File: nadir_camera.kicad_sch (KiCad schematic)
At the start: 54 parts, among them J1 MOLEX_5051102491, J12 Conn 02x05 1.27mm, J13 Micro_SD_Card, J14 USB_C_Receptacle_USB2.0, SW5 KMR2x, SW6 CAS-120TA, U24 STM32H743VITx, U25 USBLC6-2SC6, Y4 12MHz/7pF

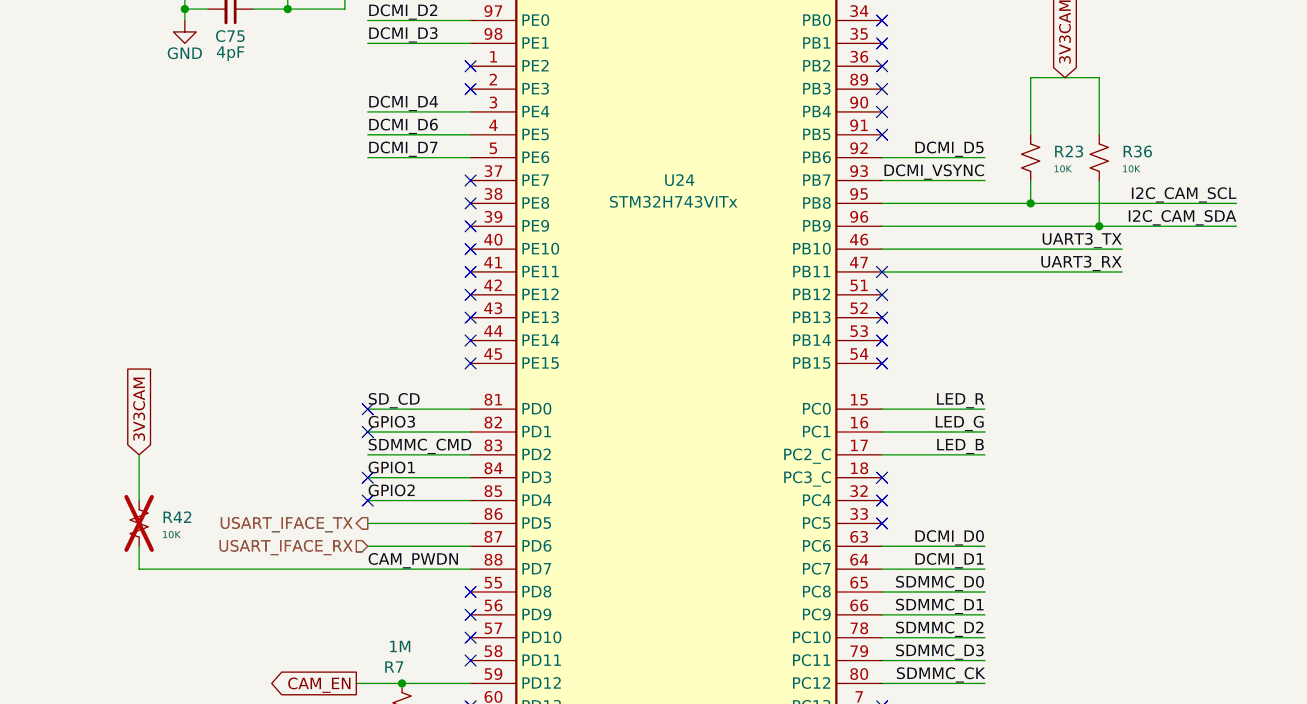
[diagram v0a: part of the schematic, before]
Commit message: Add MPNs for all parts
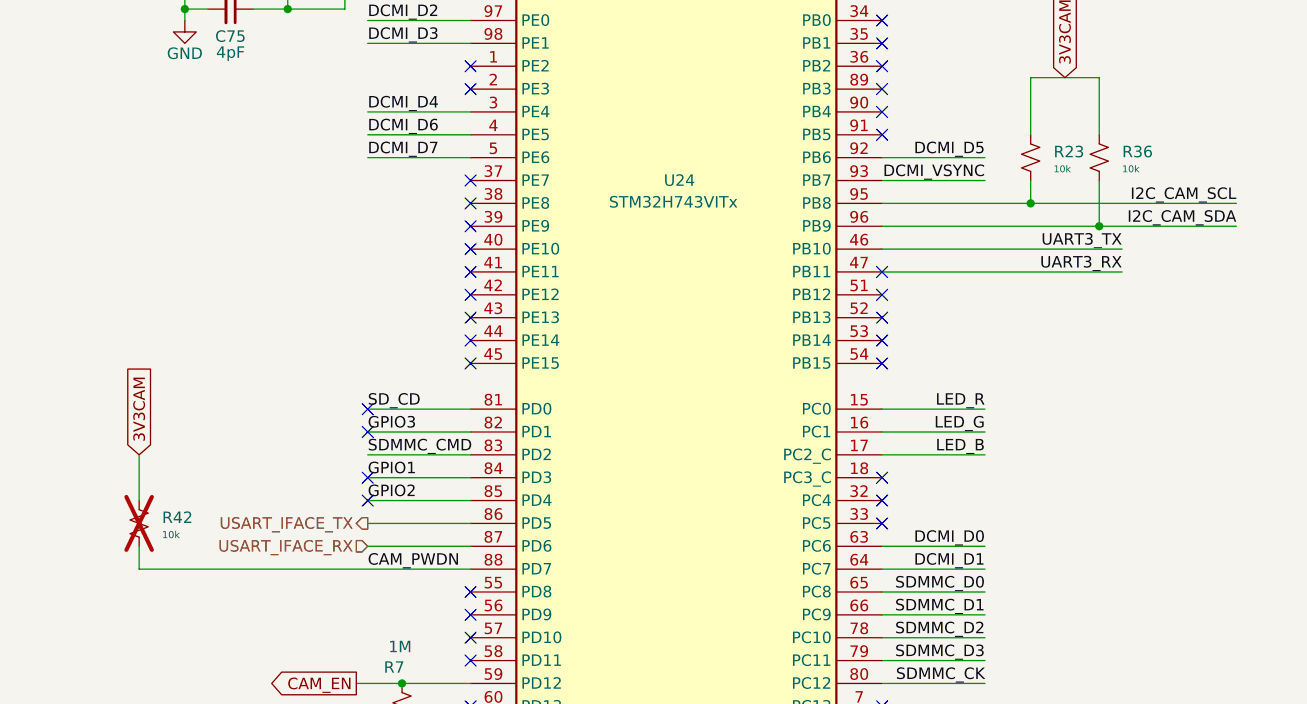
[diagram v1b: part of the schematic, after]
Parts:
- C17, C20: Manufacturer_Part_Number GRT188R61C106ME13D -> GCM188R71E105KA64D
- C62: Manufacturer_Part_Number (none) -> C1206C476M8PAC7800
- C63, C64, C65, C66, C67, C68: Manufacturer_Part_Number (none) -> GCM188L81H104KA57D
- C69: Manufacturer_Part_Number (none) -> GCM188R72A103KA37D
- C70, C71: Manufacturer_Part_Number (none) -> GCM188R71E105KA64D
- C72, C73: Manufacturer_Part_Number (none) -> GCM188R70J225KE22D
- C74, C75: Manufacturer_Part_Number (none) -> CGA3E2C0G1H040C080AA
- FB3: Manufacturer_Part_Number (none) -> BLM18SG121TZ1D
- R23, R36, R42: value 10K -> 10k; Manufacturer_Part_Number (none) -> ERJ-3EKF1002V
- R43: Manufacturer_Part_Number (none) -> ERJ-3EKF1004V
- U24: Manufacturer_Part_Number (none) -> STM32H743VIT6
- Y4: Manufacturer_Part_Number (none) -> ECS-120-7-36Q-AEY-TR
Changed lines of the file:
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@@
 			)
 		)
+		(property "Manufacturer_Part_Number" "GCM188R71E105KA64D"
+			(at 143.51 41.91 0)
+			(effects
+				(font
+					(size 1.27 1.27)
+				)
+				(hide yes)
+			)
+		)
 		(pin "1"
 		)
@@
 			)
 		)
+		(property "Manufacturer_Part_Number" "GCM188L81H104KA57D"
+			(at 35.56 41.91 0)
+			(effects
+				(font
+					(size 1.27 1.27)
+				)
+				(hide yes)
+			)
+		)
 		(pin "1"
 		)
@@
 			)
 		)
+		(property "Manufacturer_Part_Number" "GCM188R70J225KE22D"
+			(at 50.8 69.85 0)
+			(effects
+				(font
+					(size 1.27 1.27)
+				)
+				(hide yes)
+			)
+		)
 		(pin "1"
 		)
@@
 			)
 		)
+		(property "Manufacturer_Part_Number" "ERJ-3EKF1004V"
+			(at 252.73 41.91 0)
+			(effects
+				(font
+					(size 1.27 1.27)
+				)
+				(hide yes)
+			)
+		)
 		(pin "2"
 		)
@@
 			)
 		)
+		(property "Manufacturer_Part_Number" "C1206C476M8PAC7800"
+			(at 26.67 41.91 0)
+			(effects
+				(font
+					(size 1.27 1.27)
+				)
+				(hide yes)
+			)
+		)
 		(pin "1"
 		)
@@
 			)
 		)
+		(property "Manufacturer_Part_Number" "GCM188L81H104KA57D"
+			(at 85.09 41.91 0)
+			(effects
+				(font
+					(size 1.27 1.27)
+				)
+				(hide yes)
+			)
+		)
 		(pin "1"
 		)
@@
 			)
 		)
+		(property "Manufacturer_Part_Number" "CGA3E2C0G1H040C080AA"
+			(at 50.8 95.25 0)
+			(effects
+				(font
+					(size 1.27 1.27)
+				)
+				(hide yes)
+			)
+		)
 		(pin "1"
 		)
@@
 			)
 		)
-		(property "Manufacturer_Part_Number" "GRT188R61C106ME13D"
+		(property "Manufacturer_Part_Number" "GCM188R71E105KA64D"
 			(at 340.36 102.87 0)
 			(effects
@@
 			)
 		)
+		(property "Manufacturer_Part_Number" "GCM188L81H104KA57D"
+			(at 74.93 41.91 0)
+			(effects
+				(font
+					(size 1.27 1.27)
+				)
+				(hide yes)
+			)
+		)
 		(pin "1"
 		)
@@
 			)
 		)
-		(property "Manufacturer_Part_Number" "GRT188R61C106ME13D"
+		(property "Manufacturer_Part_Number" "GCM188R71E105KA64D"
 			(at 318.77 102.87 0)
 			(effects
@@
 			)
 		)
+		(property "Manufacturer_Part_Number" "GCM188R71E105KA64D"
+			(at 125.73 41.91 0)
+			(effects
+				(font
+					(size 1.27 1.27)
+				)
+				(hide yes)
+			)
+		)
 		(pin "1"
 		)
@@
 			)
 		)
+		(property "Manufacturer_Part_Number" "GCM188R72A103KA37D"
+			(at 115.57 41.91 0)
+			(effects
+				(font
+					(size 1.27 1.27)
+				)
+				(hide yes)
+			)
+		)
 		(pin "1"
 		)
@@
 			)
 		)
-		(property "Value" "10K"
+		(property "Value" "10k"
 			(at 149.86 113.03 0)
 			(effects
@@
 			)
 		)
+		(property "Manufacturer_Part_Number" "ERJ-3EKF1002V"
+			(at 147.32 111.76 0)
+			(effects
+				(font
+					(size 1.27 1.27)
+				)
+				(hide yes)
+			)
+		)
 		(pin "1"
 		)
@@
 			)
 		)
+		(property "Manufacturer_Part_Number" "GCM188L81H104KA57D"
+			(at 55.88 41.91 0)
+			(effects
+				(font
+					(size 1.27 1.27)
+				)
+				(hide yes)
+			)
+		)
 		(pin "1"
 		)
@@
 			)
 		)
+		(property "Manufacturer_Part_Number" "GCM188L81H104KA57D"
+			(at 66.04 41.91 0)
+			(effects
+				(font
+					(size 1.27 1.27)
+				)
+				(hide yes)
+			)
+		)
 		(pin "1"
 		)
@@
 			)
 		)
+		(property "Manufacturer_Part_Number" "GCM188L81H104KA57D"
+			(at 45.72 41.91 0)
+			(effects
+				(font
+					(size 1.27 1.27)
+				)
+				(hide yes)
+			)
+		)
 		(pin "1"
 		)
@@
 			)
 		)
+		(property "Manufacturer_Part_Number" "CGA3E2C0G1H040C080AA"
+			(at 50.8 85.09 0)
+			(effects
+				(font
+					(size 1.27 1.27)
+				)
+				(hide yes)
+			)
+		)
 		(pin "1"
 		)
@@
 			)
 		)
+		(property "Manufacturer_Part_Number" "STM32H743VIT6"
+			(at 100.33 114.3 0)
+			(effects
+				(font
+					(size 1.27 1.27)
+				)
+				(hide yes)
+			)
+		)
 		(pin "1"
 		)
@@
 			)
 		)
+		(property "Manufacturer_Part_Number" "BLM18SG121TZ1D"
+			(at 133.35 36.83 0)
+			(effects
+				(font
+					(size 1.27 1.27)
+				)
+				(hide yes)
+			)
+		)
 		(pin "1"
 		)
@@
 			)
 		)
+		(property "Manufacturer_Part_Number" "GCM188R70J225KE22D"
+			(at 55.88 69.85 0)
+			(effects
+				(font
+					(size 1.27 1.27)
+				)
+				(hide yes)
+			)
+		)
 		(pin "1"
 		)
@@
 			)
 		)
-		(property "Value" "10K"
+		(property "Value" "10k"
 			(at 142.24 113.03 0)
 			(effects
@@
 			)
 		)
+		(property "Manufacturer_Part_Number" "ERJ-3EKF1002V"
+			(at 139.7 111.76 0)
+			(effects
+				(font
+					(size 1.27 1.27)
+				)
+				(hide yes)
+			)
+		)
 		(pin "1"
 		)
@@
 			)
 		)
+		(property "Manufacturer_Part_Number" "ECS-120-7-36Q-AEY-TR "
+			(at 57.15 90.17 0)
+			(effects
+				(font
+					(size 1.27 1.27)
+				)
+				(hide yes)
+			)
+		)
 		(pin "1"
 		)
@@
 			)
 		)
-		(property "Value" "10K"
+		(property "Value" "10k"
 			(at 43.18 153.67 0)
 			(effects
@@
 			(at 40.64 152.4 0)
 			(effects
+				(font
+					(size 1.27 1.27)
+				)
+				(hide yes)
+			)
+		)
+		(property "Manufacturer_Part_Number" "ERJ-3EKF1002V"
+			(at 40.64 152.4 0)
+			(effects

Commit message: Fix some wrong MPNs
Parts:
- C17, C20: Manufacturer_Part_Number GCM188R71E105KA64D -> GRT188R61A106KE13D
- R63: Manufacturer_Part_Number ERJ-3EKF1002V -> ESR03EZPF1000
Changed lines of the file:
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@@
 			)
 		)
-		(property "Manufacturer_Part_Number" "ERJ-3EKF1002V"
+		(property "Manufacturer_Part_Number" "ESR03EZPF1000"
 			(at 218.44 165.1 0)
 			(effects
@@
 			)
 		)
-		(property "Manufacturer_Part_Number" "GCM188R71E105KA64D"
+		(property "Manufacturer_Part_Number" "GRT188R61A106KE13D"
 			(at 340.36 102.87 0)
 			(effects
@@
 			)
 		)
-		(property "Manufacturer_Part_Number" "GCM188R71E105KA64D"
+		(property "Manufacturer_Part_Number" "GRT188R61A106KE13D"
 			(at 318.77 102.87 0)
 			(effects

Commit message: Update to single multi-core processor
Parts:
- removed C62, C78: 47uF, Capacitor_Tantalum_SMD:CP_EIA-2012-12_Kemet-R, symbol Device:C_Polarized_Small_US
- removed C63, C64, C65, C66, C67, C68, C76, C79: 0.1uF, Capacitor_SMD:C_0603_1608Metric, symbol Device:C_Small
- removed C69: 10nF, Capacitor_SMD:C_0603_1608Metric, symbol Device:C_Small
- removed C70, C71, C77: 1uF, Capacitor_SMD:C_0603_1608Metric, symbol Device:C_Small
- removed C72, C73: 2.2uF, Capacitor_SMD:C_0603_1608Metric, symbol Device:C_Small
- removed C74, C75: 4pF, Capacitor_SMD:C_0603_1608Metric, symbol Device:C_Small
- removed C80: 4.7nF, Capacitor_SMD:C_0603_1608Metric, symbol Device:C_Small
- removed FB3: 120R, Inductor_SMD:L_0603_1608Metric, symbol Device:FerriteBead_Small
- removed J12: Conn 02x05 1.27mm, Connector_PinHeader_1.27mm:PinHeader_2x05_P1.27mm_Vertical_SMD, symbol Connector_Generic:Conn_02x05_Odd_Even
- removed J13: Micro_SD_Card, mainboard:microSD_104031-0811, symbol Connector:Micro_SD_Card_Det2
- removed J14: USB_C_Receptacle_USB2.0, Connector_USB:USB_C_Receptacle_HRO_TYPE-C-31-M-12, symbol Connector:USB_C_Receptacle_USB2.0
- removed LED6: 150141M173100, LED_SMD:LED_RGB_Wuerth-PLCC4_3.2x2.8mm_150141M173100, symbol Device:LED_ABRG
- removed R23, R36, R42, R62, R64: 10k, Resistor_SMD:R_0603_1608Metric, symbol Device:R_Small_US
- removed R43, R7: 1M, Resistor_SMD:R_0603_1608Metric, symbol Device:R_Small_US
- removed R63: 100R, Resistor_SMD:R_0603_1608Metric, symbol Device:R_Small_US
- removed R65, R66, R67, R68, R69: 47k, Resistor_SMD:R_0603_1608Metric, symbol Device:R_Small_US
- removed R70, R71: 5.1k, Resistor_SMD:R_0603_1608Metric, symbol Device:R_US
- removed R72: 1M, Resistor_SMD:R_0603_1608Metric, symbol Device:R_US
- removed RN2: 330R, Resistor_SMD:R_Array_Concave_4x0603, symbol Device:R_Pack04
- removed SW5: KMR2x, mainboard:BTN_KMR2, symbol Switch:SW_Push
- removed SW6: CAS-120TA, cameraboard:CAS-120TA, symbol Switch:SW_SPDT
- removed U24: STM32H743VITx, Package_QFP:LQFP-100_14x14mm_P0.5mm, symbol MCU_ST_STM32H7:STM32H743VITx
- removed U25: USBLC6-2SC6, Package_TO_SOT_SMD:SOT-23-6, symbol Power_Protection:USBLC6-2SC6
- removed Y4: 12MHz/7pF, Crystal:Crystal_SMD_2520-4Pin_2.5x2.0mm, symbol Device:Crystal_GND24_Small
- added C28, C29: 22pF, Capacitor_SMD:C_0603_1608Metric, symbol Device:C_Small
- added C31, C7: 0.1uF, Capacitor_SMD:C_0603_1608Metric, symbol Device:C_Small
- added C33: 0.1uF, Capacitor_SMD:C_0603_1608Metric, symbol Device:C
- added R17, R21: 10k, Resistor_SMD:R_0603_1608Metric, symbol Device:R_US
- added U23: OPT4001, Package_TO_SOT_SMD:SOT-583-8, symbol solarpanels:OPT4001
- added U5: BNO085, mainboard:BNO085, symbol mainboard:BNO085
- added Y3: 32.768kHz/12.5pF, Crystal:Crystal_SMD_MicroCrystal_CC7V-T1A-2Pin_3.2x1.5mm, symbol Device:Crystal_Small
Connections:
- net GND: now also C28.1, C29.2, C31.2, C33.2, C7.2, U23.4 (GND), U5.10 (CLKSEL0), U5.17 (H_SA0/MOSI), U5.2 (GND), U5.25 (GNDIO), U5.5 (PS1), U5.6 (PS0/WAKE)
- new net: C29.1, U5.26 (CLKSEL1/XOUT32), Y3.2
- new net: U5.1 (NC), U5.12 (NC), U5.13 (NC), U5.21 (NC), U5.22 (NC), U5.23 (NC), U5.24 (NC), U5.7 (NC), U5.8 (NC)
- new net: C28.2, U5.27 (XIN32), Y3.1
- new net: R21.1, U5.4 (BOOTN)
- new net: C7.1, U5.9 (CAP)
- new net: U23.3 (NC), U23.6 (NC)
- new net +3V3: C31.1, C33.1, R17.2, R21.2, U23.1 (VDD), U23.2 (ADDR), U5.28 (VDDIO), U5.3 (VDD)
- new net I2C_IMU_SCL: U5.19 (H_SCL/SCLK/RX)
- new net I2C_IMU_SDA: U5.20 (H_SDA/MISO/TX)
- new net I2C_LIGHT2_SCL: U23.5 (SCL)
- new net I2C_LIGHT2_SDA: U23.8 (SDA)
- new net IMU_INT: U5.14 (H_INTN)
- new net IMU_RST: R17.1, U5.11 (NRST)
- no-connect marks 51 -> 7
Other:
- note added: "IMU"
- note added: "IMU datasheet recommends 12.5pF crystal capacitance"
- note added: "Nadir Light Sensor"
- note removed: "Check Xtal Datasheet This value assumes 7pF crystal bulk capacitance"
- note removed: "Datasheet: https://www.st.com/resource/en/datasheet/stm32h743vi.pdf (See pg. 209 for power supply instructions)"
- note removed: "ESR < 100 mOhm Tol < 20%"
- note removed: "MCU (STM32H743VITx)"
- note removed: "Reset & Boot0 Switches"
- note removed: "SD Card"
- note removed: "SWD CONN"
- note removed: "See https://www.st.com/resource/en/application_note/an5612-esd-protection-of-stm32-mcus-and-mpus-stmicroelectronics.pdf, p. 22"
- note removed: "Select boot mode Set "low" for normal operation. Set "high" for bootloader mode"
- note removed: "Set for flight"
- note removed: "Shield"
- note removed: "Status LEDs"
- note removed: "Status RGB LED"
- note removed: "USB Connector"
- note removed: "USB ESD Protection"

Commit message: Add USB PD battery charging circuit
Closes #1
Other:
- moved on the sheet: C16, C17, C18, C19, C20, C21, C28, C29, C31, C33, C7, FB1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

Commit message: Move things around in schematic
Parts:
- removed C16, C19: 1uF, Capacitor_SMD:C_0603_1608Metric, symbol Device:C_Small
- removed C17, C20: 10uF, Capacitor_SMD:C_0603_1608Metric, symbol Device:C_Small
- removed C18, C21, C31, C7: 0.1uF, Capacitor_SMD:C_0603_1608Metric, symbol Device:C_Small
- removed C28, C29: 22pF, Capacitor_SMD:C_0603_1608Metric, symbol Device:C_Small
- removed C33: 0.1uF, Capacitor_SMD:C_0603_1608Metric, symbol Device:C
- removed FB1: 120R, Inductor_SMD:L_0603_1608Metric, symbol Device:FerriteBead_Small
- removed J1: MOLEX_5051102491, cameraboard:MOLEX_5051102491, symbol cameraboard:MOLEX_5051102491
- removed R17, R21: 10k, Resistor_SMD:R_0603_1608Metric, symbol Device:R_US
- removed U23: OPT4001, Package_TO_SOT_SMD:SOT-583-8, symbol solarpanels:OPT4001
- removed U5: BNO085, mainboard:BNO085, symbol mainboard:BNO085
- removed Y3: 32.768kHz/12.5pF, Crystal:Crystal_SMD_MicroCrystal_CC7V-T1A-2Pin_3.2x1.5mm, symbol Device:Crystal_Small
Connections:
- no-connect marks 7 -> 0
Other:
- note removed: "Camera Connector"
- note removed: "IMU"
- note removed: "IMU datasheet recommends 12.5pF crystal capacitance"
- note removed: "Nadir Light Sensor"
